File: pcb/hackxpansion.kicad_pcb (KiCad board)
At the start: 4 copper layers, 52 x 43 mm, 77 parts, among them CN1 533981471, CN2 533981471, CN3 533981471, CN4 533981471, IC1 ADS7128IRTET, J1 Conn_01x03_MountingPin, J2 USB_C_Receptacle_USB2.0_14P, Q1 BSS138, Q2 2N7002, SW1 SW_Push, SW2 SW_Push, SW3 SW_On_Off, U2 RP2354B, U5 SPX3819M5-L-3-3, U7 BQ24075RGT, Y1 ABM8-272-T3

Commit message: routed pcb
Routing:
- net /Main Board/RP2354B/QSPI_SS: track 5.89 -> 56.5 mm, vias 0 -> 2
- net /Main Board/ADC/mod0.MD0: track 5.30 -> 45.1 mm
- net /Main Board/ADC/mod0.MD1: track 4.60 -> 44.0 mm, vias 0 -> 1
- net /+3V3: track 270.2 -> 290.2 mm, vias 11 -> 14
- net /Main Board/Display/SCLK: track 27.6 -> 27.0 mm

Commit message: finished basic routing
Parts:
- removed CN1, CN4: 533981471, easyeda2kicad:CONN-SMD_14P-P1.25_MOLEX_533981471
- removed R18, R19, R20, R21: 10K, Resistor_SMD:R_0402_1005Metric
- removed U4, U6: ~, Connector_PinSocket_2.54mm:PinSocket_2x07_P2.54mm_Horizontal
- moved D1 0.34 mm to (152.8, 66.4)
- moved R25 0.34 mm to (151.0, 67.2)
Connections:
- CN2 pad 15: unconnected-(CN2-Pad15) -> /GND
- CN2 pad 16: unconnected-(CN2-Pad16) -> /GND
- CN3 pad 15: unconnected-(CN3-Pad15) -> /GND
- CN3 pad 16: unconnected-(CN3-Pad16) -> /GND
- FPC1 pad 13: unconnected-(FPC1-Pad13) -> /GND
- FPC1 pad 14: unconnected-(FPC1-Pad14) -> /GND
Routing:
- net /Main Board/RP2354B/RUN: track 6.18 -> 26.8 mm, vias 0 -> 2
- net /GND: track 38.1 -> 54.4 mm, vias 47 -> 63
- net /Main Board/Module Bay 0/GPIO1: track 15.1 -> 17.1 mm
- net Net-(R3-Pad1): track 1.50 -> 0.00 mm

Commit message: cleaned up routing
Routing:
- net /+3V3: track 289.9 -> 295.4 mm
- net /Main Board/RP2354B/QSPI_SS: track 56.5 -> 52.0 mm
- net /Connector Main Mod2/mod.MD0: track 32.8 -> 35.4 mm
- net /Connector Main Mod2/mod.MD1: track 33.6 -> 35.9 mm
- net /GND: track 54.4 -> 56.5 mm, vias 63 -> 66
- net /Main Board/Display/RESET: track 62.4 -> 64.4 mm
- net /Connector Main Mod2/bank.GPIO8: track 38.9 -> 37.4 mm
- net /Main Board/Module Bay 0/GPIO5: track 68.3 -> 69.6 mm
- net /Main Board/Display/SCLK: track 27.0 -> 25.9 mm
- net /Main Board/Display/MOSI: track 27.8 -> 26.7 mm
- net /Main Board/Module Bay 0/GPIO6: track 67.7 -> 68.9 mm
- net /Main Board/ADC/mod1.MD0: track 79.6 -> 80.7 mm
- net /Main Board/Module Bay 1/GPIO9: track 62.8 -> 63.7 mm
- net Net-(FPC1-Pad2): track 19.2 -> 18.3 mm
- net /Connector Main Mod3/bank.GPIO8: track 44.7 -> 43.8 mm
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
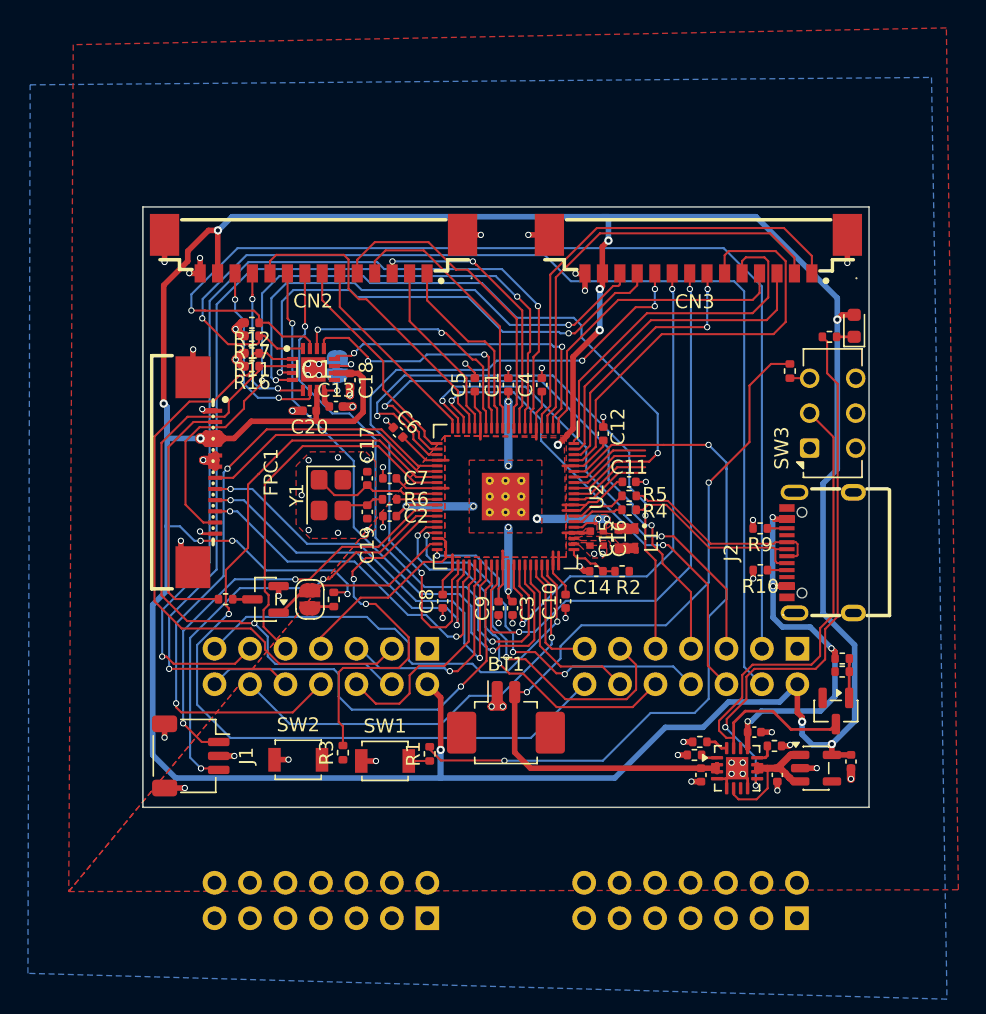
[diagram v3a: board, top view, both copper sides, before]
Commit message: added mounting holes
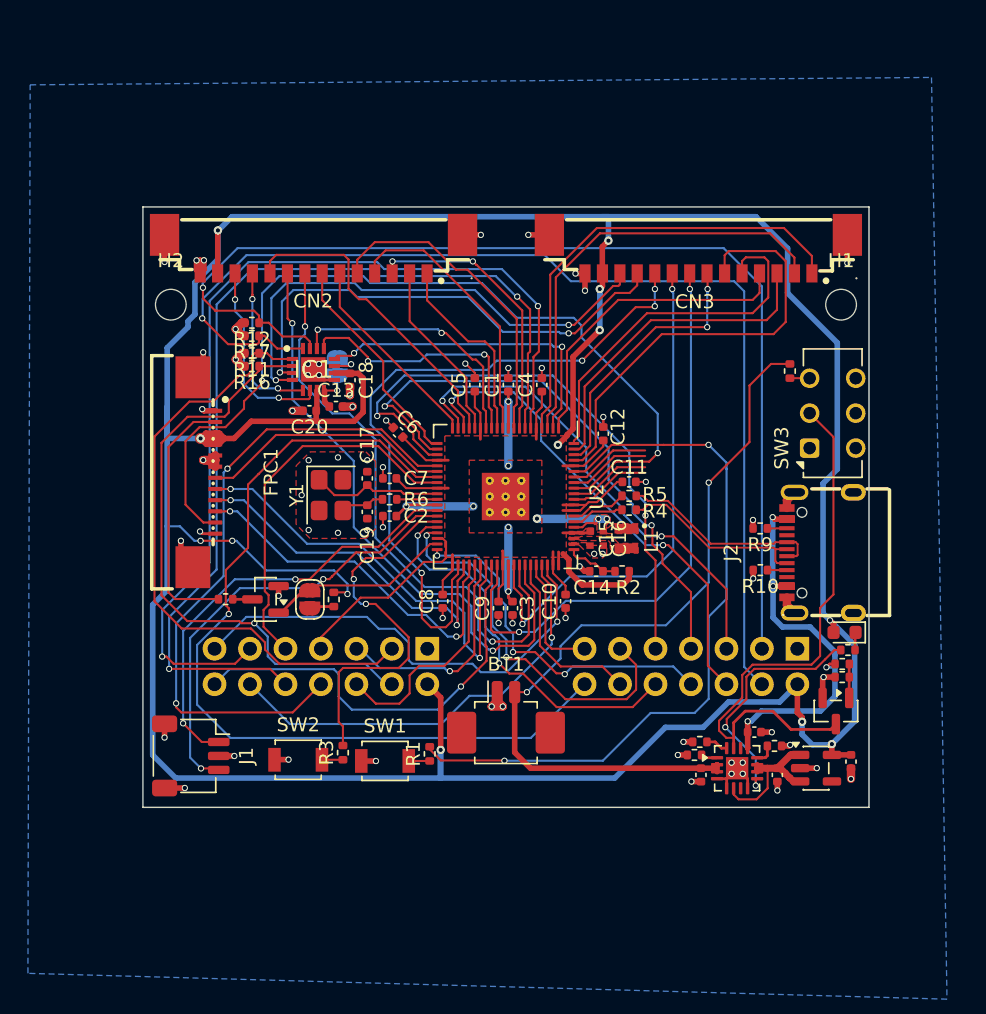
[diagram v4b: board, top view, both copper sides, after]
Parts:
- removed J3 (x2): ~, Connector_PinHeader_2.54mm:PinHeader_2x07_P2.54mm_Horizontal
- added H1: MountingHole, MountingHole:MountingHole_2.2mm_M2, F.Cu at (151.9, 64.9)
- added H2: MountingHole, MountingHole:MountingHole_2.2mm_M2, F.Cu at (103.9, 64.9)
- moved R25 22.5 mm to (152.4, 89.6)
- moved D1 22.0 mm to (152.1, 88.4), turned to 180 degrees
- moved R13 0.39 mm to (152.0, 90.6)
- moved R14 0.39 mm to (151.9, 91.6)
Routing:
- net Net-(U7-~{CHG}): track 39.9 -> 17.4 mm
- net /GND: track 56.5 -> 65.1 mm, vias 66 -> 67
- net /+3V3: track 295.4 -> 301.3 mm, vias 14 -> 13
- net /Main Board/ADC/mod1.MD0: track 80.7 -> 79.0 mm
- net Net-(R3-Pad1): track 0.00 -> 1.50 mm

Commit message: added some stitching vias
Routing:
- net /GND: vias 67 -> 248
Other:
- board text added: "{ "ViaStitching": "0.2", "stitch_zone_0": { "HSpacing": "1", "VSpacing": "1", "HOffset": "0", "VOffset": "0", "Clearance": "0", "Randomize": false } }"
- board text added: "{ "ViaStitching": "0.2", "stitch_zone_0": { "HSpacing": "1", "VSpacing": "1", "HOffset": "0", "VOffset": "0", "Clearance": "0.2", "Randomize": false } }"
- board text added: "{ "ViaStitching": "0.2", "stitch_zone_0": { "HSpacing": "1", "VSpacing": "1", "HOffset": "0", "VOffset": "0", "Clearance": "0.25", "Randomize": false } }"
- board text added: "{ "ViaStitching": "0.2", "stitch_zone_0": { "HSpacing": "1", "VSpacing": "1.25", "HOffset": "0", "VOffset": "0", "Clearance": "0.25", "Randomize": false } }"

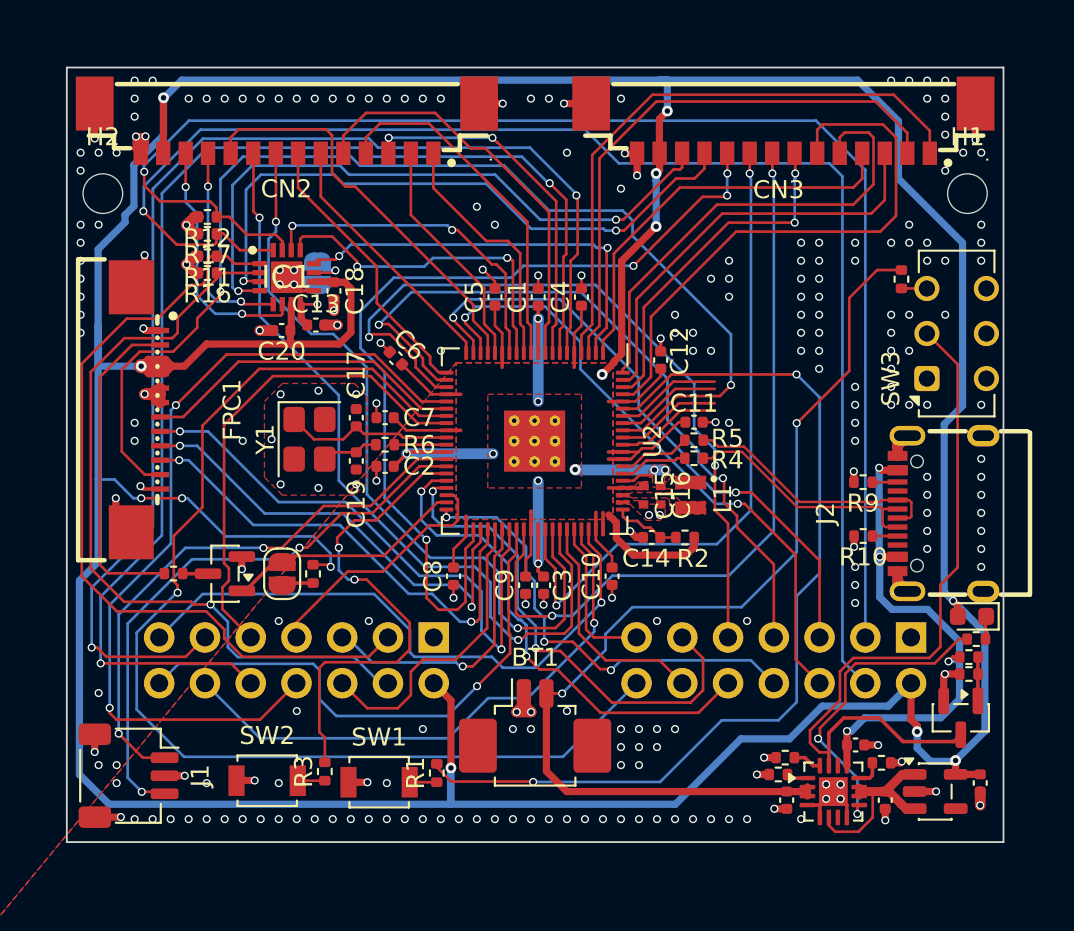
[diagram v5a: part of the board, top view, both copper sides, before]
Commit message: added more stitching vias
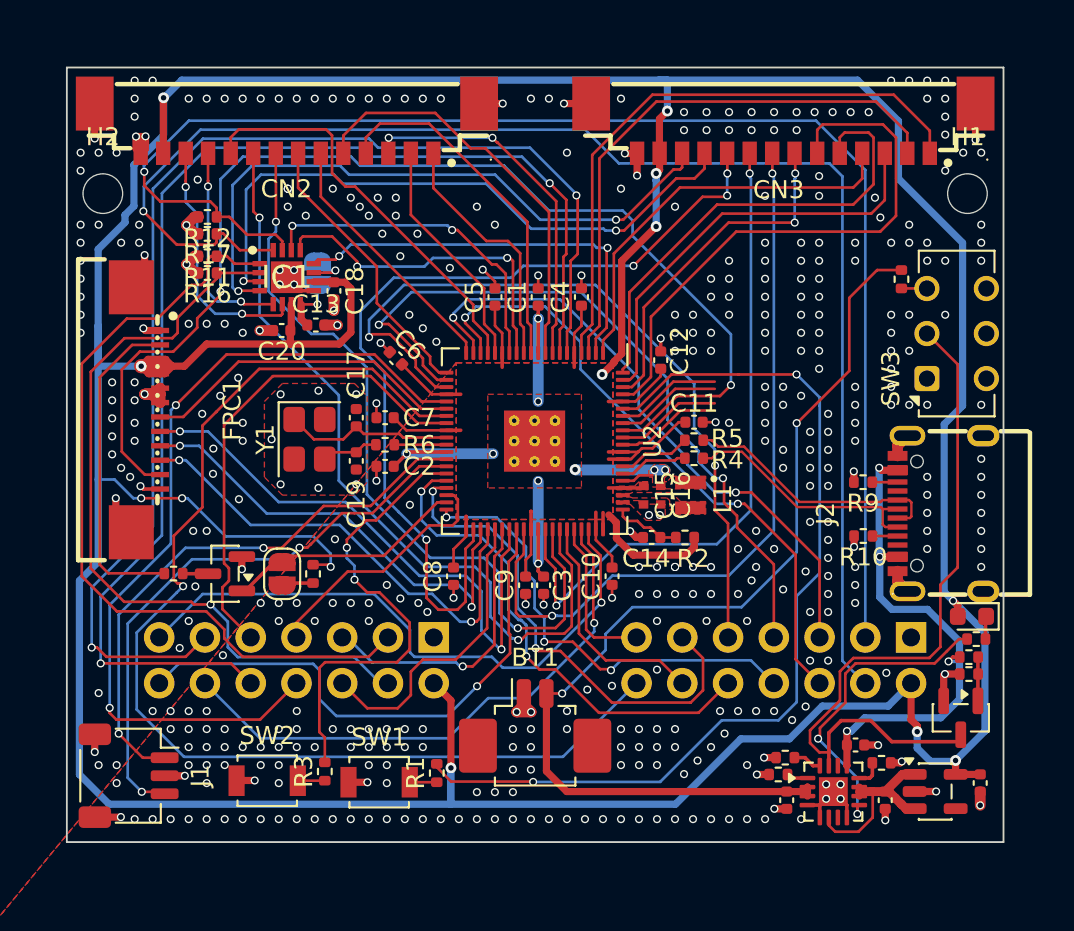
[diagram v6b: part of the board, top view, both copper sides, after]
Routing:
- net /Main Board/RP2354B/RUN: track 26.8 -> 25.8 mm
- net /GND: vias 248 -> 451

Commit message: added test points
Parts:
- added TP1: TestPoint, TestPoint:TestPoint_Pad_D1.0mm, F.Cu at (126.0, 66.7)
- added TP10: TestPoint, TestPoint:TestPoint_Pad_D1.0mm, B.Cu at (103.7, 83.3)
- added TP11: TestPoint, TestPoint:TestPoint_Pad_D1.0mm, F.Cu at (139.1, 76.8)
- added TP12: TestPoint, TestPoint:TestPoint_Pad_D1.0mm, B.Cu at (136.0, 71.9)
- added TP13: TestPoint, TestPoint:TestPoint_Pad_D1.0mm, B.Cu at (137.6, 73.4)
- added TP14: TestPoint, TestPoint:TestPoint_Pad_D1.0mm, B.Cu at (138.8, 77.9)
- added TP2: TestPoint, TestPoint:TestPoint_Pad_D1.0mm, F.Cu at (122.2, 65.9)
- added TP3: TestPoint, TestPoint:TestPoint_Pad_D1.0mm, B.Cu at (120.8, 68.7)
- added TP4: TestPoint, TestPoint:TestPoint_Pad_D1.0mm, B.Cu at (112.6, 82.3)
- added TP5: TestPoint, TestPoint:TestPoint_Pad_D1.0mm, B.Cu at (110.2, 81.9)
- added TP6: TestPoint, TestPoint:TestPoint_Pad_D1.0mm, B.Cu at (110.0, 74.8)
- added TP7: TestPoint, TestPoint:TestPoint_Pad_D1.0mm, B.Cu at (111.9, 79.7)
- added TP8: TestPoint, TestPoint:TestPoint_Pad_D1.0mm, F.Cu at (108.5, 80.8)
- added TP9: TestPoint, TestPoint:TestPoint_Pad_D1.0mm, B.Cu at (151.6, 99.5)
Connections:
- U2 pad 70: unconnected-(U2-QSPI_SD3-Pad70) -> Net-(U2-QSPI_SD3)
- U2 pad 71: unconnected-(U2-QSPI_SCLK-Pad71) -> Net-(U2-QSPI_SCLK)
- U2 pad 73: unconnected-(U2-QSPI_SD2-Pad73) -> Net-(U2-QSPI_SD2)
- U2 pad 74: unconnected-(U2-QSPI_SD1-Pad74) -> Net-(U2-QSPI_SD1)
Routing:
- net Net-(U2-QSPI_SD1): track 0.00 -> 10.2 mm, vias 0 -> 1
- net Net-(U2-QSPI_SD2): track 0.00 -> 9.15 mm, vias 0 -> 1
- net Net-(U2-QSPI_SD3): track 0.00 -> 7.29 mm, vias 0 -> 1
- net Net-(U2-QSPI_SCLK): track 0.00 -> 7.25 mm
- net unconnected-(U2-QSPI_SD1-Pad74): track 5.89 -> 0.00 mm
- net unconnected-(U2-QSPI_SD2-Pad73): track 5.89 -> 0.00 mm
- net unconnected-(U2-QSPI_SCLK-Pad71): track 5.89 -> 0.00 mm
- net unconnected-(U2-QSPI_SD3-Pad70): track 5.89 -> 0.00 mm
- net /Main Board/Power/REG-OUT: track 10.8 -> 13.9 mm, vias 0 -> 1
- net /Main Board/Display/RESET: track 64.4 -> 66.7 mm
- net /Main Board/ADC/ALERT: track 22.9 -> 25.0 mm, vias 2 -> 3
- net /Main Board/ADC/SDA: track 18.8 -> 20.3 mm
- net /Main Board/Display/DC: track 18.2 -> 18.8 mm, vias 0 -> 1
- net /GND: vias 451 -> 441

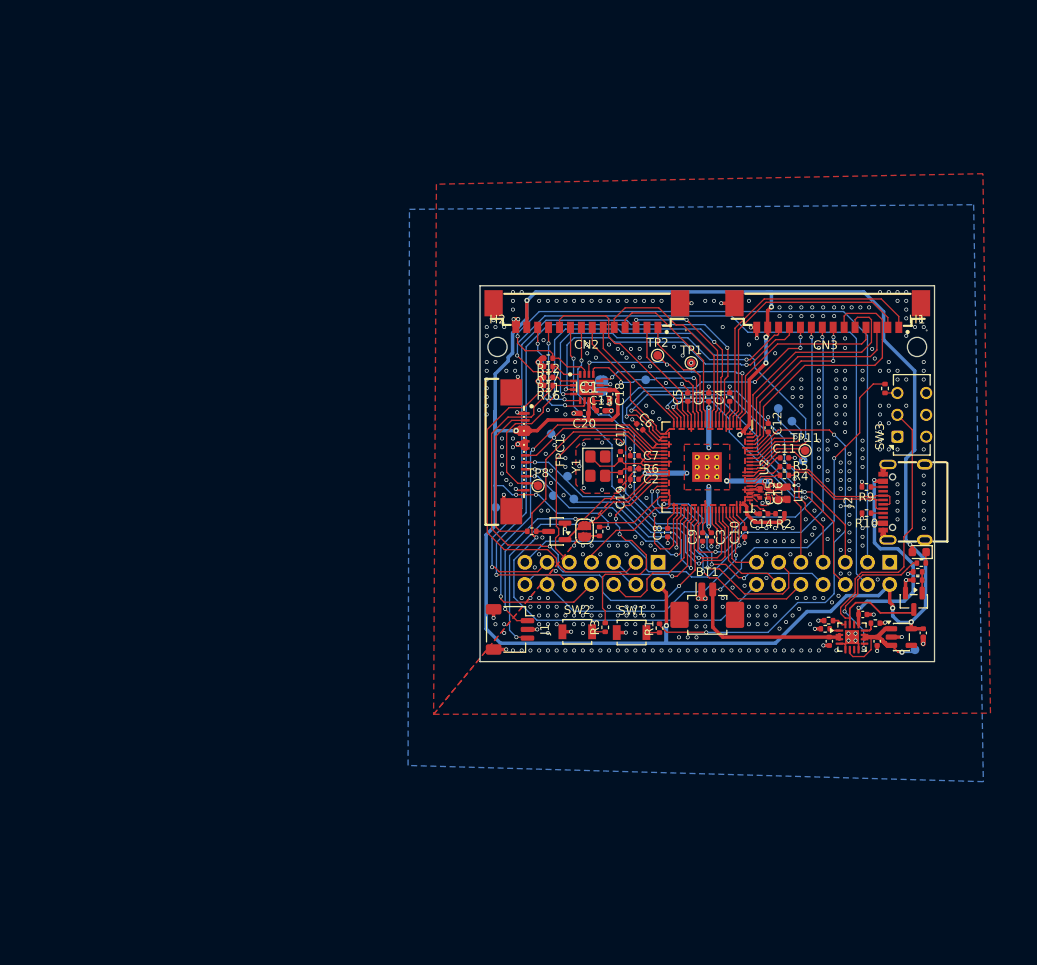
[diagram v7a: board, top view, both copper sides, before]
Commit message: laid out secound module
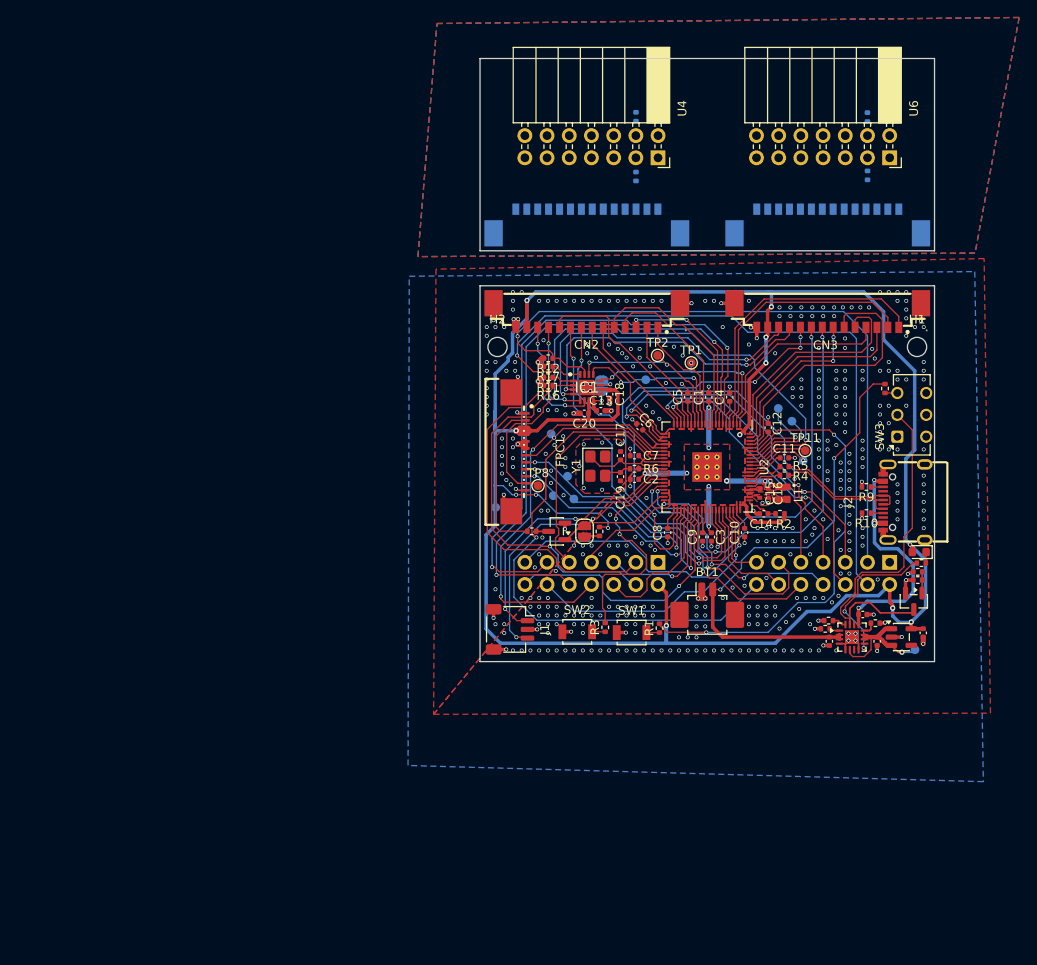
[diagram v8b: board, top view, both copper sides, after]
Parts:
- added CN1: 533981471, easyeda2kicad:CONN-SMD_14P-P1.25_MOLEX_533981471, B.Cu at (114.1, 50.5)
- added CN4: 533981471, easyeda2kicad:CONN-SMD_14P-P1.25_MOLEX_533981471, B.Cu at (141.6, 50.5)
- added R18: 10K, Resistor_SMD:R_0402_1005Metric, B.Cu at (119.7, 38.6)
- added R19: 10K, Resistor_SMD:R_0402_1005Metric, B.Cu at (146.2, 38.6)
- added R20: 10K, Resistor_SMD:R_0402_1005Metric, B.Cu at (119.7, 45.4)
- added R21: 10K, Resistor_SMD:R_0402_1005Metric, B.Cu at (146.2, 45.3)
- added U4: ~, Connector_PinSocket_2.54mm:PinSocket_2x07_P2.54mm_Horizontal, F.Cu at (122.2, 43.3)
- added U6: ~, Connector_PinSocket_2.54mm:PinSocket_2x07_P2.54mm_Horizontal, F.Cu at (148.7, 43.3)
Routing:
- net /GND: vias 441 -> 440
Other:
- board size 52 x 43 mm -> 52 x 69 mm
